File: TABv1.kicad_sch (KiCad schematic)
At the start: 37 parts, among them J10 Conn_02x03_Odd_Even, J11 Conn_UART_1, J5 Conn_02x06_Counter_Clockwise, J6 SWD, J9 Conn_02x03_Odd_Even, Q2 NMOS, SW2 RESET, U1 RP2350B-QFN80, Y1 12MHz

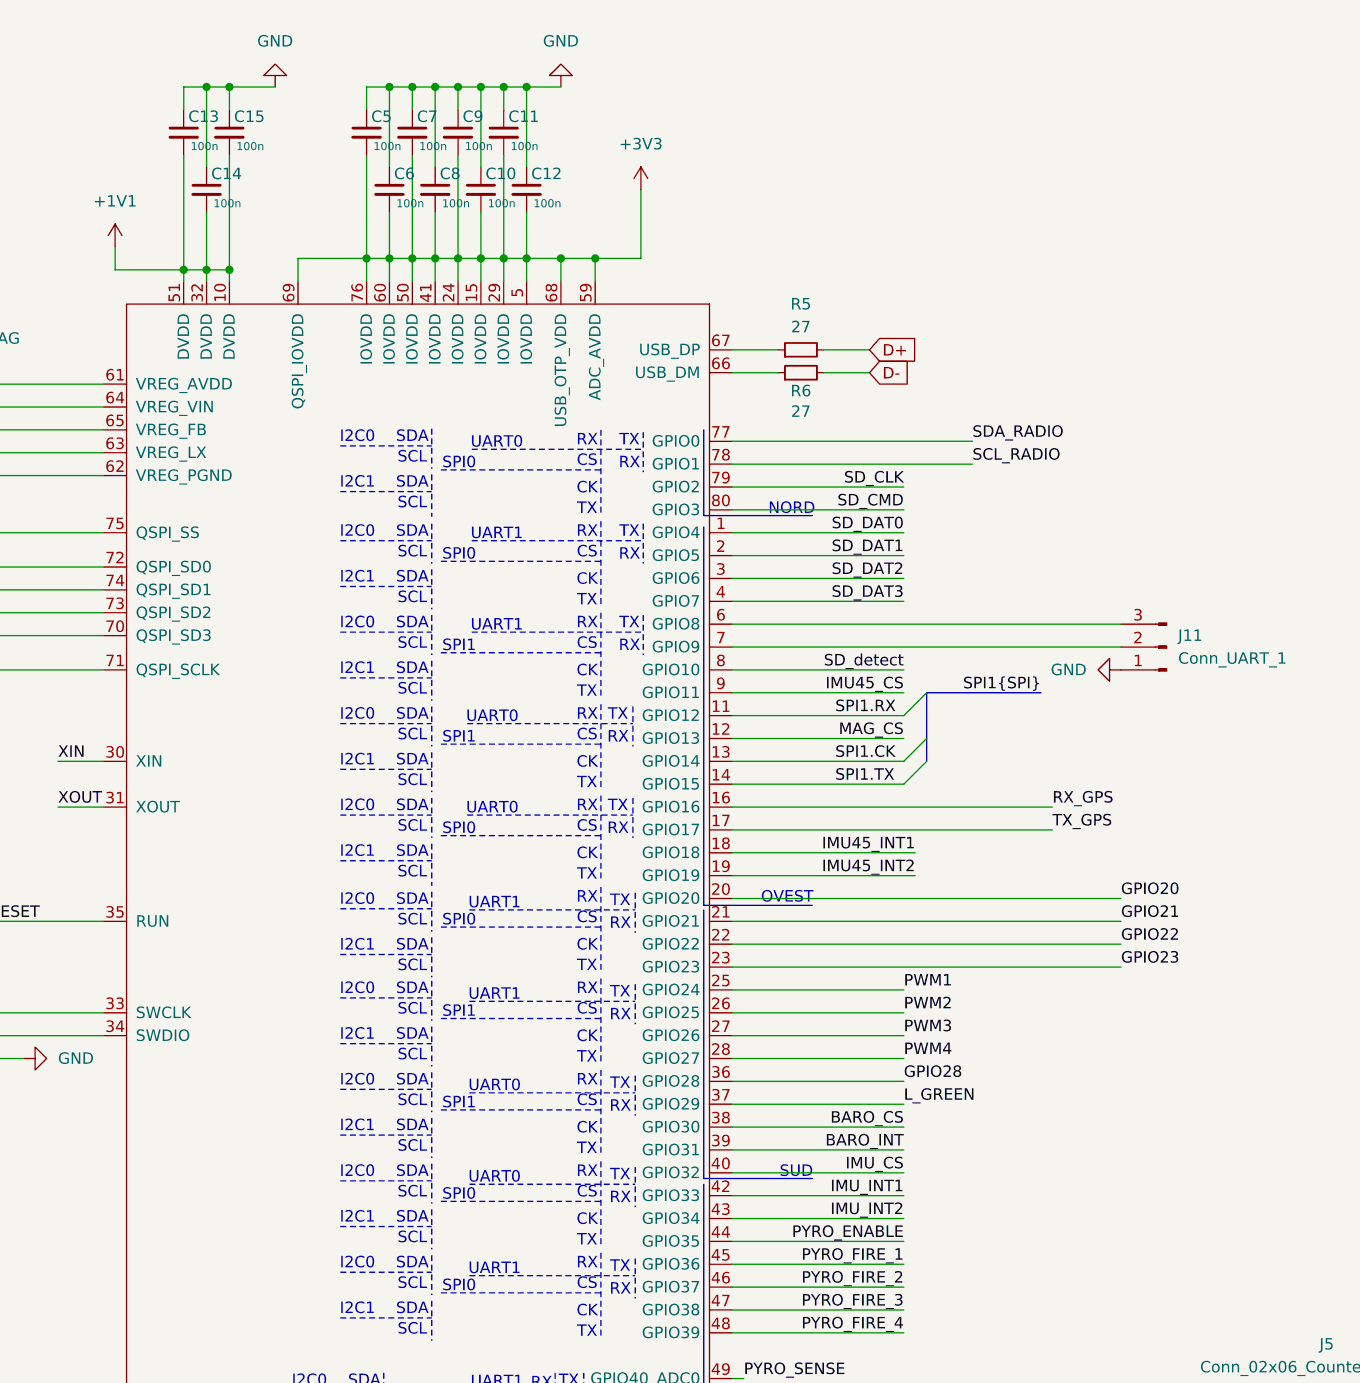
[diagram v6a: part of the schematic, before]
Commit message: mega routing sensori led e 5v usb
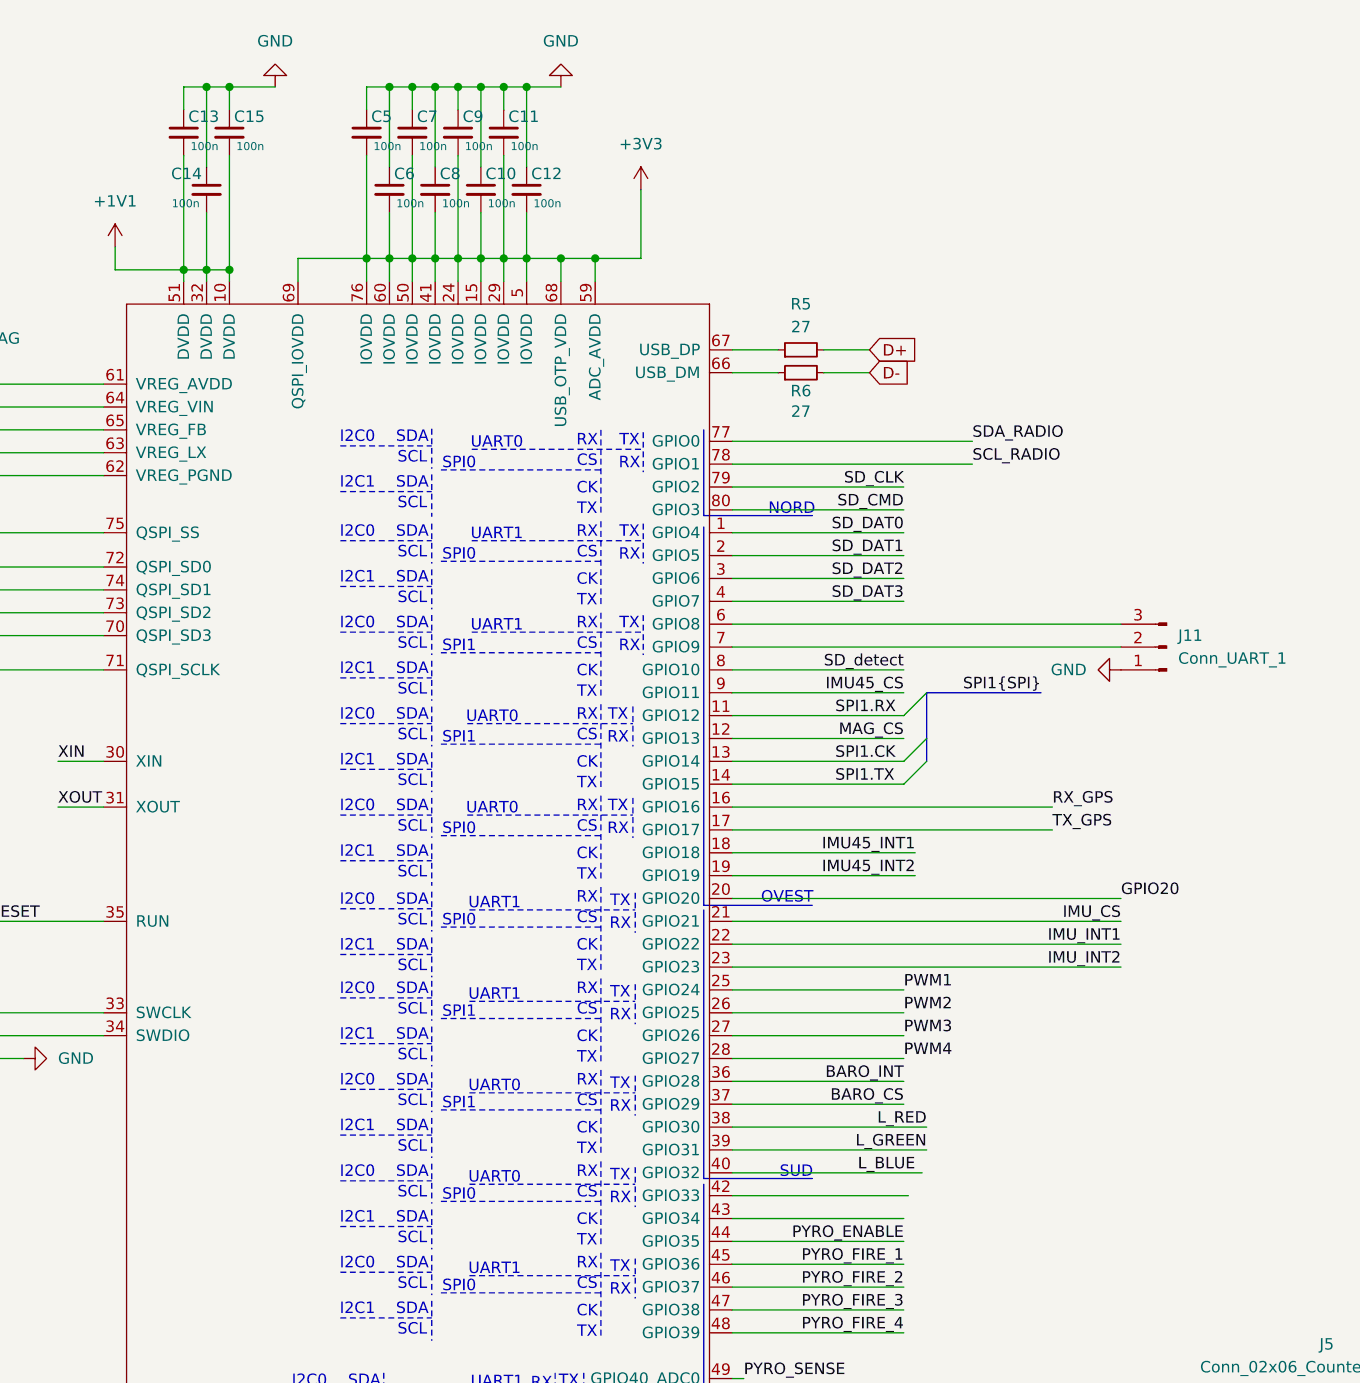
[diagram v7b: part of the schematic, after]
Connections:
- net BARO_CS: now also U1.37 (GPIO29); no longer U1.38 (GPIO30)
- net BARO_INT: now also U1.36 (GPIO28); no longer U1.39 (GPIO31)
- net GPIO21: no longer U1.21 (GPIO21)
- net GPIO22: no longer U1.22 (GPIO22)
- net GPIO23: no longer U1.23 (GPIO23)
- net GPIO28: no longer U1.36 (GPIO28)
- net IMU_CS: now also U1.21 (GPIO21); no longer U1.40 (GPIO32)
- net IMU_INT1: now also U1.22 (GPIO22); no longer U1.42 (GPIO33)
- net IMU_INT2: now also U1.23 (GPIO23); no longer U1.43 (GPIO34)
- net L_BLUE: now also U1.40 (GPIO32)
- net L_GREEN: now also U1.39 (GPIO31); no longer U1.37 (GPIO29)
- net L_RED: now also U1.38 (GPIO30)
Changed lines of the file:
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@@
 	(wire
 		(pts
-			(xy 147.32 170.18) (xy 166.37 170.18)
+			(xy 147.32 170.18) (xy 168.402 170.18)
 		)
 		(stroke
@@
 	(wire
 		(pts
-			(xy 147.32 172.72) (xy 166.37 172.72)
+			(xy 147.32 172.72) (xy 166.878 172.72)
 		)
 		(stroke
@@
 	(wire
 		(pts
-			(xy 147.32 165.1) (xy 166.37 165.1)
+			(xy 147.32 165.1) (xy 168.91 165.1)
 		)
 		(stroke
@@
 	(wire
 		(pts
-			(xy 147.32 167.64) (xy 166.37 167.64)
+			(xy 147.32 167.64) (xy 168.91 167.64)
 		)
 		(stroke
@@
 		)
 	)
-	(label "GPIO28"
-		(at 166.37 160.02 0)
+	(label "BARO_INT"
+		(at 166.37 160.02 180)
 		(effects
 			(font
 				(size 1.27 1.27)
 			)
-			(justify left bottom)
+			(justify right bottom)
 		)
 	)
@@
 		)
 	)
-	(label "IMU_INT2"
-		(at 166.37 175.26 180)
-		(effects
-			(font
-				(size 1.27 1.27)
-			)
-			(justify right bottom)
-		)
-	)
 	(label "MAG_CS"
 		(at 166.37 121.92 180)
@@
 		)
 	)
+	(label "IMU_INT1"
+		(at 190.5 144.78 180)
+		(effects
+			(font
+				(size 1.27 1.27)
+			)
+			(justify right bottom)
+		)
+	)
 	(label "{QSPI}"
 		(at 41.91 95.25 0)
@@
 		)
 	)
+	(label "IMU_INT2"
+		(at 190.5 147.32 180)
+		(effects
+			(font
+				(size 1.27 1.27)
+			)
+			(justify right bottom)
+		)
+	)
 	(label "SD_DAT0"
 		(at 313.69 144.78 0)
@@
 		)
 	)
+	(label "BARO_CS"
+		(at 166.37 162.56 180)
+		(effects
+			(font
+				(size 1.27 1.27)
+			)
+			(justify right bottom)
+		)
+	)
 	(label "GPIO20"
 		(at 190.5 139.7 0)
@@
 		)
 	)
-	(label "GPIO22"
-		(at 190.5 144.78 0)
+	(label "L_BLUE"
+		(at 167.64 170.18 180)
 		(effects
 			(font
 				(size 1.27 1.27)
 			)
-			(justify left bottom)
+			(justify right bottom)
 		)
 	)
@@
 		)
 	)
-	(label "GPIO21"
-		(at 190.5 142.24 0)
-		(effects
-			(font
-				(size 1.27 1.27)
-			)
-			(justify left bottom)
-		)
-	)
 	(label "RX_GPS"
 		(at 182.88 129.54 0)
@@
 		)
 	)
-	(label "IMU_CS"
-		(at 166.37 170.18 180)
-		(effects
-			(font
-				(size 1.27 1.27)
-			)
-			(justify right bottom)
-		)
-	)
 	(label "SPI1.CK"
 		(at 158.75 124.46 0)
@@
 		)
 	)
-	(label "BARO_INT"
-		(at 166.37 167.64 180)
-		(effects
-			(font
-				(size 1.27 1.27)
-			)
-			(justify right bottom)
-		)
-	)
 	(label "MAG_CS"
 		(at 217.17 125.73 0)
@@
 		)
 	)
-	(label "PYRO_FIRE_4"
-		(at 246.38 166.37 0)
+	(label "IMU_CS"
+		(at 190.5 142.24 180)
 		(effects
 			(font
 				(size 1.27 1.27)
 			)
-			(justify left bottom)
+			(justify right bottom)
 		)
 	)
-	(label "GPIO23"
-		(at 190.5 147.32 0)
+	(label "PYRO_FIRE_4"
+		(at 246.38 166.37 0)
 		(effects
 			(font
@@
 		)
 	)
-	(label "BARO_CS"
-		(at 166.37 165.1 180)
+	(label "L_GREEN"
+		(at 168.91 167.64 180)
 		(effects
 			(font
@@
 		)
 	)
-	(label "L_GREEN"
-		(at 166.37 162.56 0)
+	(label "L_RED"
+		(at 168.91 165.1 180)
 		(effects
 			(font
 				(size 1.27 1.27)
 			)
-			(justify left bottom)
+			(justify right bottom)
 		)
 	)
@@
 		)
 	)
-	(label "IMU_INT1"
-		(at 166.37 172.72 180)
-		(effects
-			(font
-				(size 1.27 1.27)
-			)
-			(justify right bottom)
-		)
-	)
 	(label "L_BLUE"
 		(at 353.314 186.69 180)
@@
 		(lib_id "Device:C_Small")
 		(at 88.9 60.96 0)
+		(mirror y)
 		(unit 1)
 		(exclude_from_sim no)
@@
 		(dnp no)
 		(property "Reference" "C14"
-			(at 89.408 59.182 0)
+			(at 88.392 59.182 0)
 			(effects
 				(font
@@
 		)
 		(property "Value" "100n"
-			(at 89.662 62.484 0)
+			(at 88.138 62.484 0)
 			(effects
 				(font

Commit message: Changes 11/12
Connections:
- net BUZZ: now also U1.42 (GPIO33); no longer U1.57 (GPIO46_ADC6)
- net L_BLUE: no longer U1.56 (GPIO45_ADC5)
- net PWM1: now also J10.2 (Pin_2); no longer J9.2 (Pin_2)
- net PWM2: now also J10.1 (Pin_1); no longer J9.1 (Pin_1)
- net PWM3: now also J9.2 (Pin_2); no longer J10.2 (Pin_2)
- net PWM4: now also J9.1 (Pin_1); no longer J10.1 (Pin_1)
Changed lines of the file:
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@@
 	(wire
 		(pts
-			(xy 147.32 172.72) (xy 166.878 172.72)
+			(xy 147.32 172.72) (xy 167.64 172.72)
 		)
 		(stroke
@@
 		)
 	)
-	(label "PWM3"
-		(at 360.68 101.6 0)
-		(effects
-			(font
-				(size 1.27 1.27)
-			)
-			(justify left bottom)
-		)
-	)
 	(label "GPIO41"
 		(at 166.37 195.58 0)
@@
 		)
 	)
+	(label "PWM1"
+		(at 360.68 101.6 0)
+		(effects
+			(font
+				(size 1.27 1.27)
+			)
+			(justify left bottom)
+		)
+	)
 	(label "SD_detect"
 		(at 166.37 114.3 180)
@@
 	)
 	(label "PWM2"
-		(at 342.9 85.09 180)
-		(effects
-			(font
-				(size 1.27 1.27)
-			)
-			(justify right bottom)
-		)
-	)
-	(label "PWM2"
 		(at 166.37 152.4 0)
 		(effects
@@
 		)
 	)
-	(label "IMU45_INT2"
-		(at 217.17 123.19 0)
+	(label "PWM4"
+		(at 342.9 85.09 180)
 		(effects
 			(font
 				(size 1.27 1.27)
 			)
-			(justify left bottom)
+			(justify right bottom)
 		)
 	)
-	(label "BUZZ"
-		(at 166.37 208.28 0)
+	(label "IMU45_INT2"
+		(at 217.17 123.19 0)
 		(effects
 			(font
@@
 		)
 	)
+	(label "PWM3"
+		(at 360.68 85.09 0)
+		(effects
+			(font
+				(size 1.27 1.27)
+			)
+			(justify left bottom)
+		)
+	)
 	(label "SCL_RADIO"
 		(at 177.8 254 180)
@@
 		)
 	)
-	(label "SPI1.CK"
-		(at 158.75 124.46 0)
+	(label "BUZZ"
+		(at 167.64 172.72 0)
 		(effects
 			(font
@@
 		)
 	)
-	(label "PWM1"
-		(at 360.68 85.09 0)
+	(label "SPI1.CK"
+		(at 158.75 124.46 0)
 		(effects
 			(font
@@
 		)
 	)
+	(label "PWM2"
+		(at 342.9 101.6 180)
+		(effects
+			(font
+				(size 1.27 1.27)
+			)
+			(justify right bottom)
+		)
+	)
 	(label "SD0"
 		(at 57.15 102.87 0)
@@
 		)
 	)
-	(label "PWM4"
-		(at 342.9 101.6 180)
-		(effects
-			(font
-				(size 1.27 1.27)
-			)
-			(justify right bottom)
-		)
-	)
 	(label "GPIO28"
 		(at 207.01 208.28 180)
@@
 		)
 	)
-	(label "L_BLUE"
-		(at 166.37 205.74 0)
-		(effects
-			(font
-				(size 1.27 1.27)
-			)
-			(justify left bottom)
-		)
-	)
